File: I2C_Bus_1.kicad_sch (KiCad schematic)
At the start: 12 parts, among them U3 ICM-42688-P, U5 LIS3MDL, U6 SHT4x

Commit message: Added buttons, LEDs, TPs, and Miku
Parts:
- removed R7, R8: I2C, Resistor_SMD:R_0603_1608Metric, symbol Device:R
- added R18, R21: I2C, Resistor_SMD:R_0603_1608Metric, symbol Device:R
- C1, C12, C2, C6: value 100n -> 0.1u
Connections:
- net +3V3: now also R18.1, R21.1
- net I2C_1_SCL: now also R21.2
- net I2C_1_SDA: now also R18.2
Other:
- note added: "Bus pull-up resistors"
- note added: "Bus speed 1MHz (Fast Mode+)"

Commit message: Added I2C resistor values
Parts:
- R18, R21: value I2C -> 1k
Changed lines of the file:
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@@
 			)
 		)
-		(property "Value" "I2C"
+		(property "Value" "1k"
 			(at 211.836 115.57 0)
 			(effects
@@
 			)
 		)
-		(property "Value" "I2C"
+		(property "Value" "1k"
 			(at 219.456 115.57 0)
 			(effects

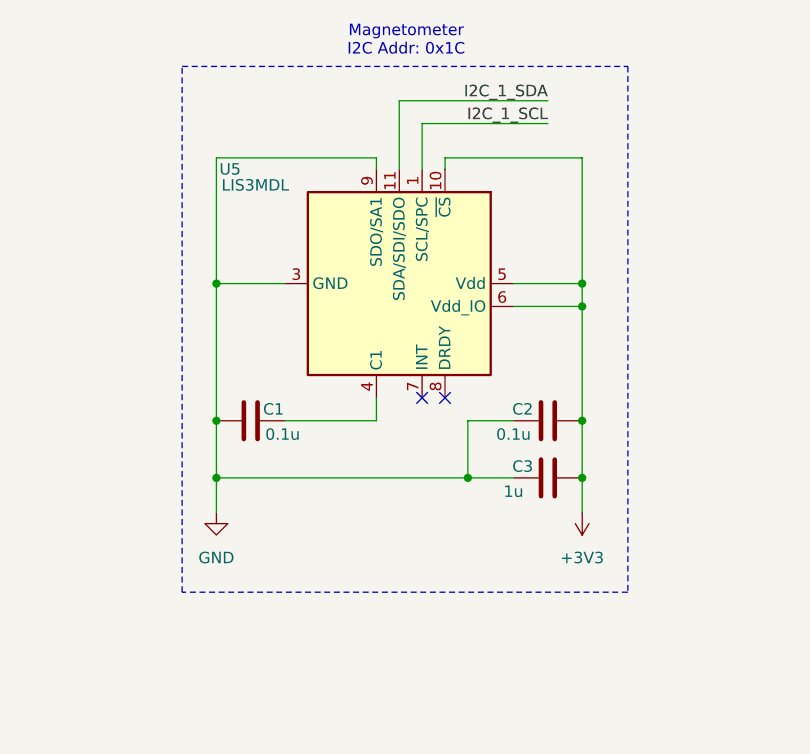
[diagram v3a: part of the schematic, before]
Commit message: Moved LIS3MDL to FM bus
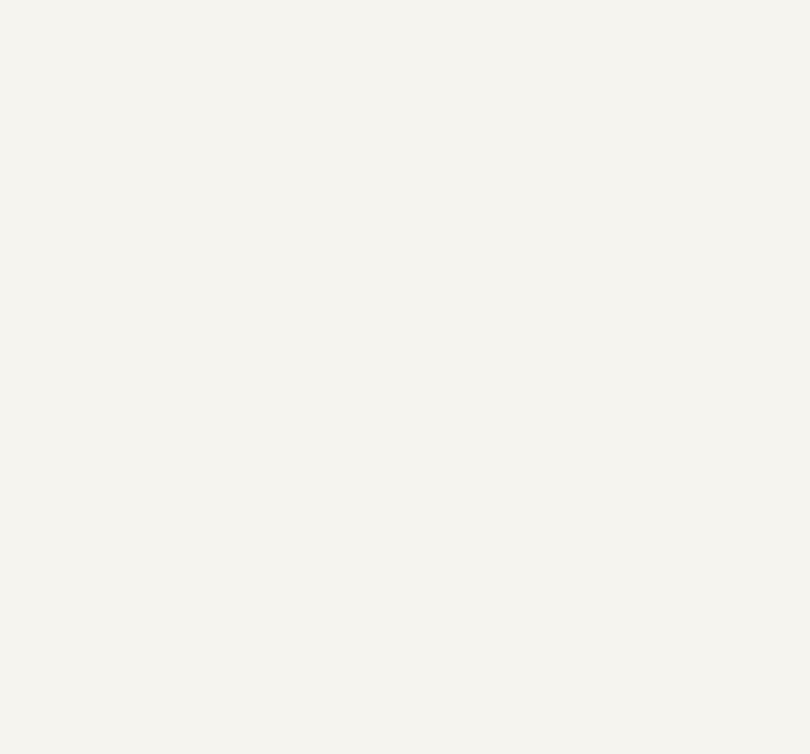
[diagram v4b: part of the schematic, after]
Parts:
- removed C1, C2: 0.1u, Capacitor_SMD:C_0603_1608Metric, symbol Device:C
- removed C3: 1u, Capacitor_SMD:C_0603_1608Metric, symbol Device:C
- removed U5: LIS3MDL, Package_LGA:LGA-12_2x2mm_P0.5mm, symbol Sensor_Magnetic:LIS3MDL
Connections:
- no-connect marks 8 -> 6
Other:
- note removed: "Magnetometer I2C Addr: 0x1C"
